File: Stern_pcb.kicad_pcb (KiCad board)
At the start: 4 copper layers, 50 x 50 mm, 51 parts, among them J1 Conn_01x05, J2 Conn_01x06, J3 Conn_01x04, J4 Conn_01x02, Q1 DMG3404L, U1 STM32G071KBTx, U2 MIC5504-3.3YM5, U3 BQ25895RTW

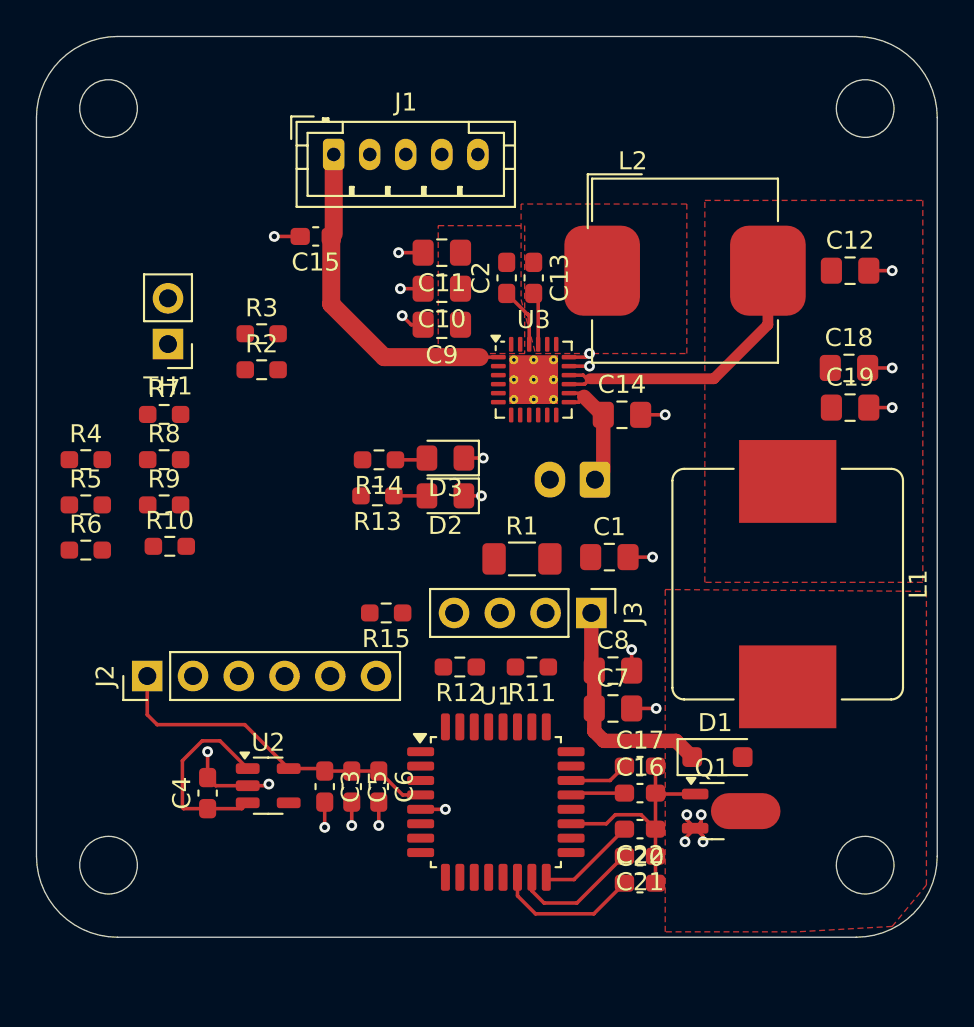
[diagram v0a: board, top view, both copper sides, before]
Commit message: marked unused capaacitors as not placed. Pull down on gate channel
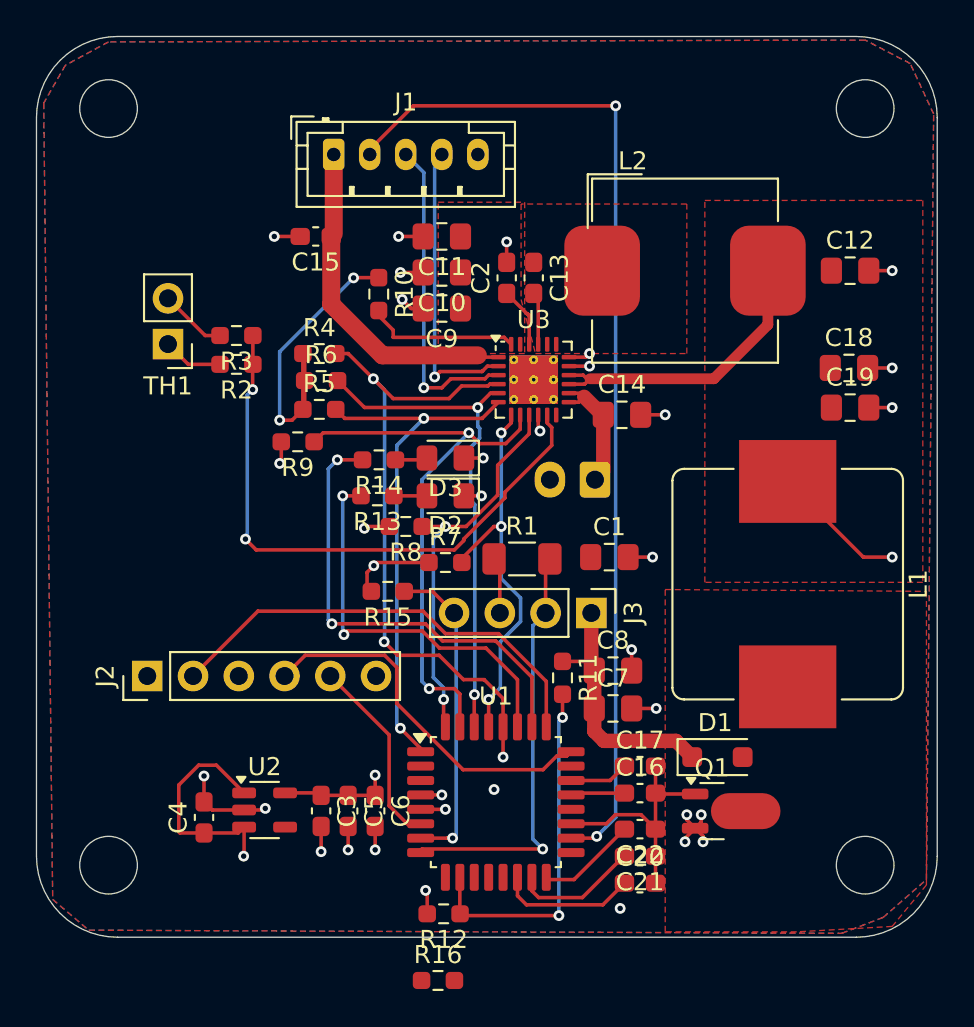
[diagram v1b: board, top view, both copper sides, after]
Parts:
- added R16: 10k, Resistor_SMD:R_0603_1608Metric_Pad0.98x0.95mm_HandSolder, F.Cu at (142.8, 118.9)
- moved R10 18.2 mm to (139.5, 80.8), turned to -90 degrees
- moved R7 17.6 mm to (143.2, 95.7)
- moved R6 16.1 mm to (136.3, 85.6)
- moved R4 14.2 mm to (136.2, 84.1)
- moved R5 14.0 mm to (136.2, 87.2)
- moved R8 13.9 mm to (141.0, 93.7), turned to 180 degrees
- moved R12 13.7 mm to (143.1, 115.2)
- moved R9 8.20 mm to (135.0, 89.0), turned to 180 degrees
- moved R11 1.80 mm to (149.7, 102.1), turned to -90 degrees
- moved R2 1.43 mm to (131.6, 84.7), turned to 180 degrees
- moved R3 1.40 mm to (131.6, 83.1), turned to 180 degrees
- moved U2 1.36 mm to (133.2, 109.4)
- moved C3 1.36 mm to (136.3, 109.5)
- moved C4 1.36 mm to (129.8, 109.8)
- moved C5 1.36 mm to (137.8, 109.5)
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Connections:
- net DSEL renamed Net-(U3-DSEL)
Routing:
- net VSYS: track 27.7 -> 89.6 mm, vias 0 -> 2
- net CC1: track 0.00 -> 57.4 mm, vias 0 -> 2
- net STAT: track 0.00 -> 36.4 mm, vias 0 -> 3
- net Net-(U3-TS): track 0.00 -> 33.1 mm, vias 0 -> 2
- net OTG: track 0.00 -> 32.1 mm, vias 0 -> 2
- net SDA: track 0.00 -> 29.3 mm, vias 0 -> 2
- net SCL: track 0.00 -> 28.0 mm, vias 0 -> 2
- net Net-(U1-PA15): track 0.00 -> 25.9 mm, vias 0 -> 2
- net SYS_SWCLK: track 0.00 -> 25.2 mm
- net I_SNS: track 0.00 -> 23.7 mm, vias 0 -> 1
- net Net-(U1-PB3): track 0.00 -> 22.2 mm, vias 0 -> 2
- net INT: track 0.00 -> 21.9 mm, vias 0 -> 3
- net CE: track 0.00 -> 21.8 mm, vias 0 -> 2
- net SYS_SWDIO: track 0.00 -> 20.6 mm
- net U_SNS: track 0.00 -> 19.9 mm, vias 0 -> 2
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- added copper zone on In2.Cu, net +3V3
- added copper zone on B.Cu, net GND
- added copper zone on F.Cu, net GND
- added copper zone on In2.Cu, net GND

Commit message: Verbindung zum Temperatursensor war falsch
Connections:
- R2 pad 1: Net-(U3-TS) -> Net-(U3-REGN)
- R2 pad 2: Net-(R2-Pad2) -> Net-(U3-TS)
- TH1 pad 1: Net-(R2-Pad2) -> Net-(U3-TS)
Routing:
- net Net-(U3-TS): track 33.1 -> 36.5 mm
- net Net-(R2-Pad2): track 3.35 -> 0.00 mm
